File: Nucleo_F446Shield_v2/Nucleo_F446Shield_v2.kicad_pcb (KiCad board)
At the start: 2 copper layers, 85 x 97.4 mm, 49 parts, among them J1 Barrel_Jack, J19 I2C3, J2 Conn_02x13_Odd_Even, J20 UART4, J21 xt60 male, J3 CAN1, J4 CAN2, SW1 SW1, SW11 DIP1, SW2 SW2, SW3 SW3, U1 NUCLEO-F446RE, U2 MP1584, U3 TJA1050, U4 TJA1050

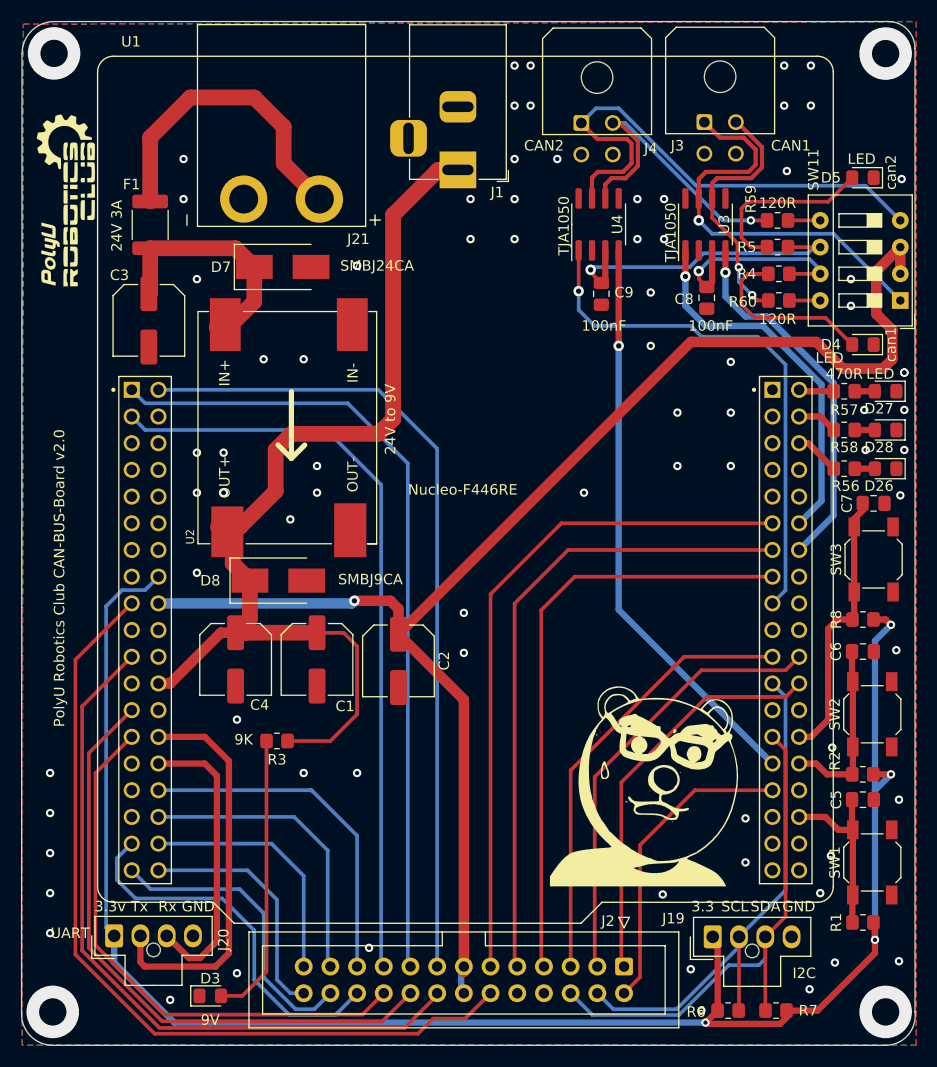
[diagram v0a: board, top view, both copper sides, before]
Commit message: power connector added
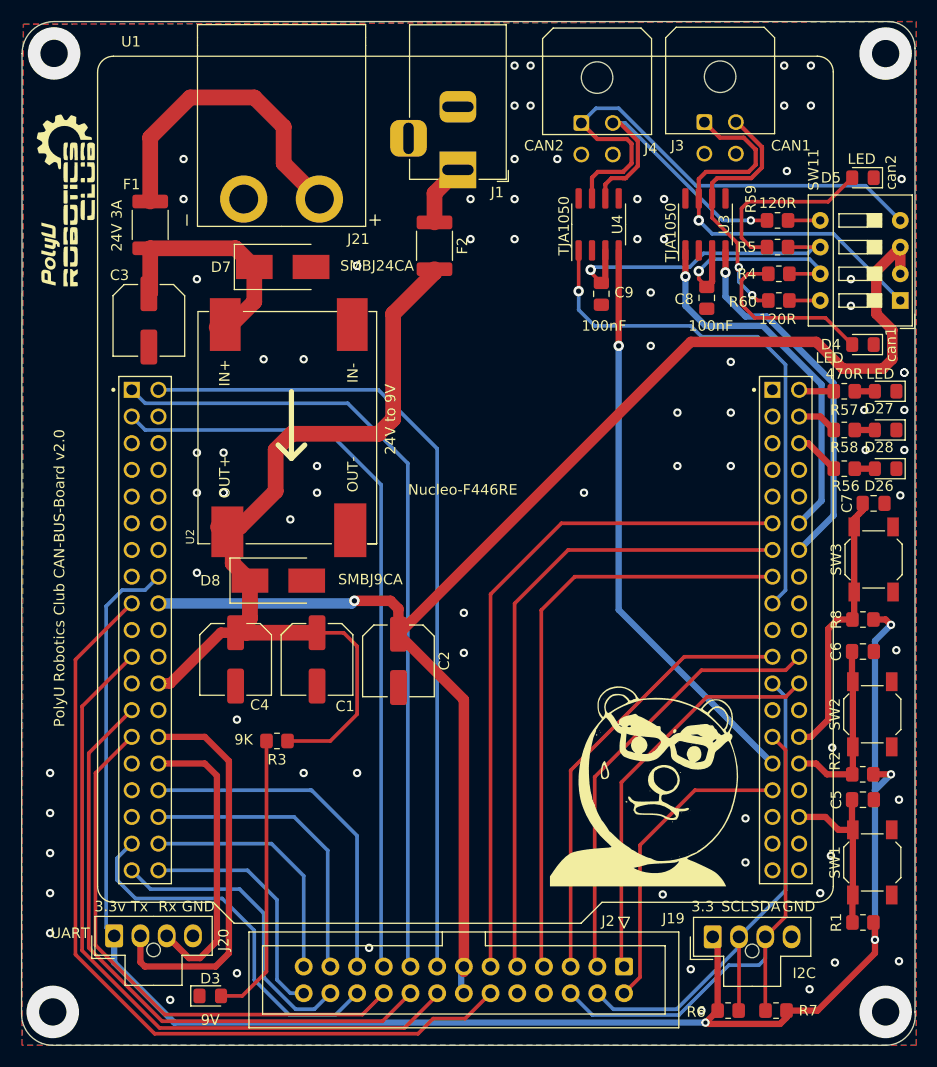
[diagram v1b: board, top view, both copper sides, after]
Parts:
- added F2: 24V 3A, Fuse:Fuse_1812_4532Metric_Pad1.30x3.40mm_HandSolder, F.Cu at (83.6, 55.2)
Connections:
- J1 pad 1: VCC -> Net-(J1-Pad1)
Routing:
- net VCC: track 98.5 -> 87.0 mm
- net Net-(J1-Pad1): track 0.00 -> 5.92 mm
